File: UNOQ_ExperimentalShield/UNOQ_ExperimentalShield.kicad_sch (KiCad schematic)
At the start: 72 parts, among them CN1 485, CN2 USB, CN3 Can, CN4 Can, CN5 485, J1 Power, J2 Digital/PWM, J3 Analog, J4 Digital/PWM, SW1 Usr1, SW2 Usr1, U1 25LCxxx, U2 TMP102xxDRL, U3 MAX3485ESA-MS, U4 CH340N, U5 TJA1051T-3, U7 ATECC608A-SSHDA

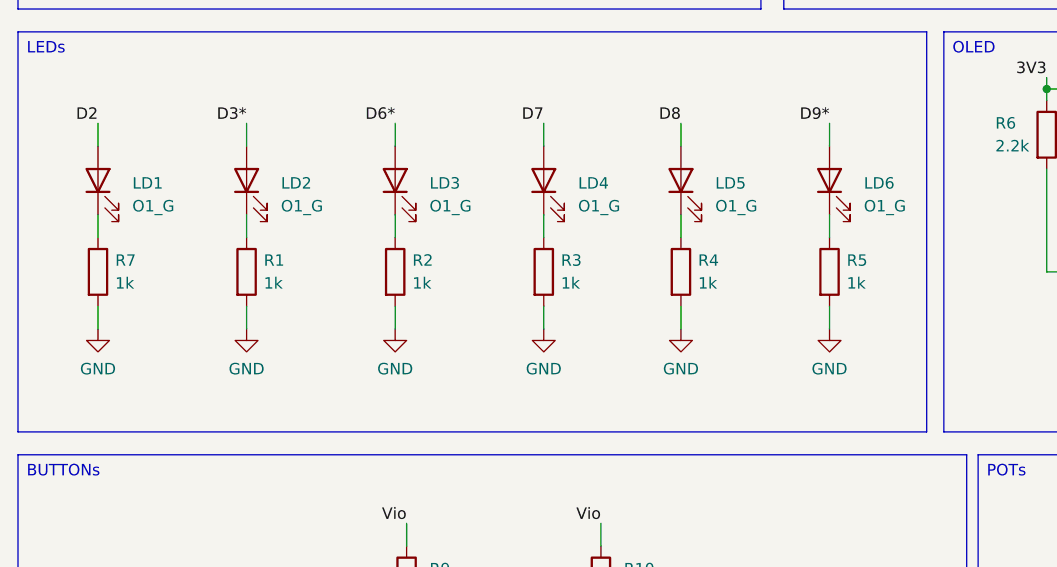
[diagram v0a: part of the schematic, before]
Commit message: Added unoq (without can) test sketch
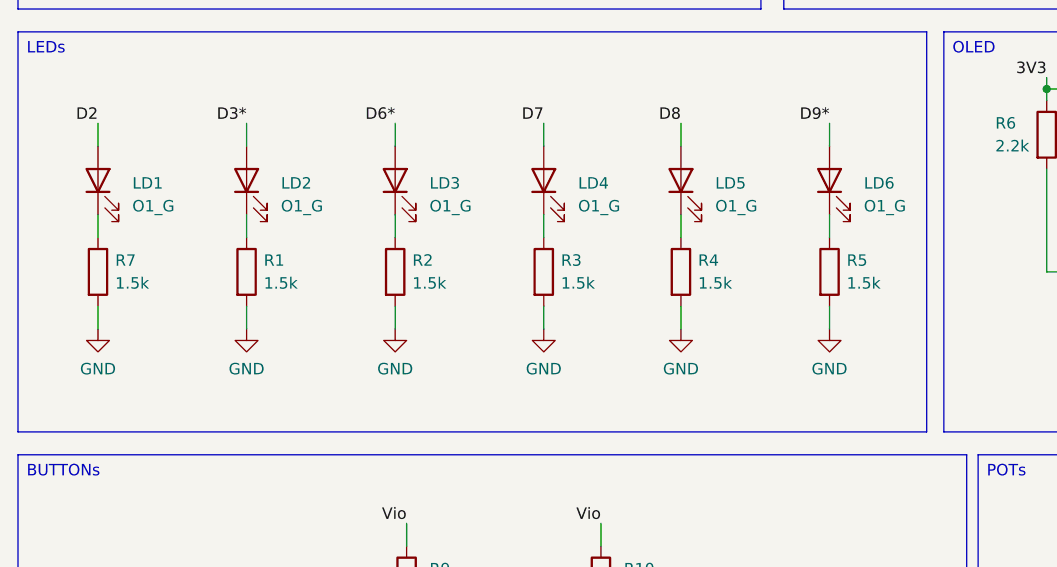
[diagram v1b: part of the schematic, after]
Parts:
- J1, J4: footprint Connector_PinSocket_2.54mm:PinSocket_1x08_P2.54mm_Vertical -> Connector_PinHeader_2.54mm:PinHeader_1x08_P2.54mm_Vertical; LCSC (none) -> C32713274
- J2: footprint Connector_PinSocket_2.54mm:PinSocket_1x10_P2.54mm_Vertical -> Connector_PinHeader_2.54mm:PinHeader_1x10_P2.54mm_Vertical; LCSC (none) -> C57369
- J3: footprint Connector_PinSocket_2.54mm:PinSocket_1x06_P2.54mm_Vertical -> Connector_PinHeader_2.54mm:PinHeader_1x06_P2.54mm_Vertical; LCSC (none) -> C32713272
- R1, R2, R3, R4, R5, R7: value 1k -> 1.5k; LCSC C140196 -> C25867
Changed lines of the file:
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@@
 			)
 		)
-		(property "Footprint" "Connector_PinSocket_2.54mm:PinSocket_1x08_P2.54mm_Vertical"
+		(property "Footprint" "Connector_PinHeader_2.54mm:PinHeader_1x08_P2.54mm_Vertical"
 			(at 44.45 46.99 0)
 			(effects
@@
 			)
 		)
+		(property "Note" ""
+			(at 44.45 46.99 0)
+			(effects
+				(font
+					(size 1.27 1.27)
+				)
+				(hide yes)
+			)
+		)
+		(property "LCSC" "C32713274"
+			(at 44.45 46.99 0)
+			(effects
+				(font
+					(size 1.27 1.27)
+				)
+				(hide yes)
+			)
+		)
 		(pin "1"
 		)
@@
 			)
 		)
-		(property "Footprint" "Connector_PinSocket_2.54mm:PinSocket_1x10_P2.54mm_Vertical"
+		(property "Footprint" "Connector_PinHeader_2.54mm:PinHeader_1x10_P2.54mm_Vertical"
 			(at 62.23 44.45 0)
 			(effects
@@
 			)
 		)
+		(property "Note" ""
+			(at 62.23 44.45 0)
+			(effects
+				(font
+					(size 1.27 1.27)
+				)
+				(hide yes)
+			)
+		)
+		(property "LCSC" "C57369"
+			(at 62.23 44.45 0)
+			(effects
+				(font
+					(size 1.27 1.27)
+				)
+				(hide yes)
+			)
+		)
 		(pin "1"
 		)
@@
 			)
 		)
-		(property "Footprint" "Connector_PinSocket_2.54mm:PinSocket_1x06_P2.54mm_Vertical"
+		(property "Footprint" "Connector_PinHeader_2.54mm:PinHeader_1x06_P2.54mm_Vertical"
 			(at 44.45 72.39 0)
 			(effects
@@
 			)
 		)
+		(property "Note" ""
+			(at 44.45 72.39 0)
+			(effects
+				(font
+					(size 1.27 1.27)
+				)
+				(hide yes)
+			)
+		)
+		(property "LCSC" "C32713272"
+			(at 44.45 72.39 0)
+			(effects
+				(font
+					(size 1.27 1.27)
+				)
+				(hide yes)
+			)
+		)
 		(pin "1"
 		)
@@
 			)
 		)
-		(property "Footprint" "Connector_PinSocket_2.54mm:PinSocket_1x08_P2.54mm_Vertical"
+		(property "Footprint" "Connector_PinHeader_2.54mm:PinHeader_1x08_P2.54mm_Vertical"
 			(at 62.23 74.93 0)
 			(effects
@@
 			)
 		)
+		(property "Note" ""
+			(at 62.23 74.93 0)
+			(effects
+				(font
+					(size 1.27 1.27)
+				)
+				(hide yes)
+			)
+		)
+		(property "LCSC" "C32713274"
+			(at 62.23 74.93 0)
+			(effects
+				(font
+					(size 1.27 1.27)
+				)
+				(hide yes)
+			)
+		)
 		(pin "1"
 		)
@@
 			)
 		)
-		(property "Value" "1k"
+		(property "Value" "1.5k"
 			(at 48.895 128.2699 0)
 			(effects
@@
 			)
 		)
-		(property "LCSC" "C140196"
+		(property "LCSC" "C25867"
 			(at 46.99 127 0)
 			(effects
@@
 			)
 		)
-		(property "Value" "1k"
+		(property "Value" "1.5k"
 			(at 97.155 128.2699 0)
 			(effects
@@
 			)
 		)
-		(property "LCSC" "C140196"
+		(property "LCSC" "C25867"
 			(at 95.25 127 0)
 			(effects
@@
 			)
 		)
+		(property "Note" ""
+			(at 306.07 43.18 0)
+			(effects
+				(font
+					(size 1.27 1.27)
+				)
+				(hide yes)
+			)
+		)
 		(pin "3"
 		)
@@
 			)
 		)
-		(property "Value" "1k"
+		(property "Value" "1.5k"
 			(at 81.915 128.2699 0)
 			(effects
@@
 			)
 		)
-		(property "LCSC" "C140196"
+		(property "LCSC" "C25867"
 			(at 80.01 127 0)
 			(effects
@@
 			)
 		)
-		(property "Value" "1k"
+		(property "Value" "1.5k"
 			(at 65.405 128.2699 0)
 			(effects
@@
 			)
 		)
-		(property "LCSC" "C140196"
+		(property "LCSC" "C25867"
 			(at 63.5 127 0)
 			(effects
@@
 			)
 		)
-		(property "Value" "1k"
+		(property "Value" "1.5k"
 			(at 32.385 128.2699 0)
 			(effects
@@
 			)
 		)
-		(property "LCSC" "C140196"
+		(property "LCSC" "C25867"
 			(at 30.48 127 0)
 			(effects
@@
 			)
 		)
-		(property "Value" "1k"
+		(property "Value" "1.5k"
 			(at 113.665 128.2699 0)
 			(effects
@@
 			)
 		)
-		(property "LCSC" "C140196"
+		(property "LCSC" "C25867"
 			(at 111.76 127 0)
 			(effects
